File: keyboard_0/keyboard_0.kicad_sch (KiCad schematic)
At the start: 21 parts, among them J1 USB_C_Receptacle_USB2.0, U1 STM32F072CBT6, U2 PRTR5V0U2X, U3 XC6206PxxxMR-Regulator_Linear

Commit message: latest changes - incomplete routing
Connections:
- net A10 renamed ROW0
- net A3 renamed ROW2
- net A4 renamed COL13
- net A5 renamed COL12
- net A6 renamed COL11
- net A7 renamed COL10
- net A8 renamed COL1
- net A9 renamed COL0
- net B0 renamed COL9
- net B1 renamed COL8
- net B10 renamed COL6
- net B11 renamed COL5
- net B12 renamed COL4
- net B13 renamed ROW1
- net B14 renamed COL3
- net B15 renamed COL2
- net B2 renamed COL7

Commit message: connect rest of switches and bring in aux components
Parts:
- added SW1: RotaryEncoder_Switch, PCM_marbastlib-various:ROT_Alps_EC11E-Switch, symbol Device:RotaryEncoder_Switch
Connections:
- net B5 is gone; now on net COL14: U1.41 (PB5)
- net B6 is gone; now on net ROW4: U1.42 (PB6)
- net B7 is gone; now on net ROW3: U1.43 (PB7)
- net COL12: now also U1.13 (PA3); no longer U1.15 (PA5)
- net COL13: now also U1.15 (PA5); no longer U1.14 (PA4)
- net COL4: now also U1.26 (PB13); no longer U1.25 (PB12)
- net GND: now also SW1.C, SW1.S2
- net ROW1: now also U1.25 (PB12); no longer U1.26 (PB13)
- net ROW2: now also U1.14 (PA4); no longer U1.13 (PA3)
- net VBUS: now also SW1.A
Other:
- added sheet LEDs (switches.kicad_sch)

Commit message: bring back switches and separate sub sheets
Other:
- sheet LEDs: file switches.kicad_sch -> led_matrix.kicad_sch
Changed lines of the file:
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@@
 	)
 	(sheet
-		(at 165.1 77.47)
-		(size 50.165 36.83)
+		(at 161.925 73.025)
+		(size 64.135 42.545)
 		(exclude_from_sim no)
 		(in_bom yes)
@@
 		)
 		(property "Sheetname" "LEDs"
-			(at 165.1 76.7584 0)
+			(at 161.925 72.3134 0)
 			(effects
 				(font
@@
 			)
 		)
-		(property "Sheetfile" "switches.kicad_sch"
-			(at 165.1 114.8846 0)
+		(property "Sheetfile" "led_matrix.kicad_sch"
+			(at 161.925 116.1546 0)
 			(effects
 				(font

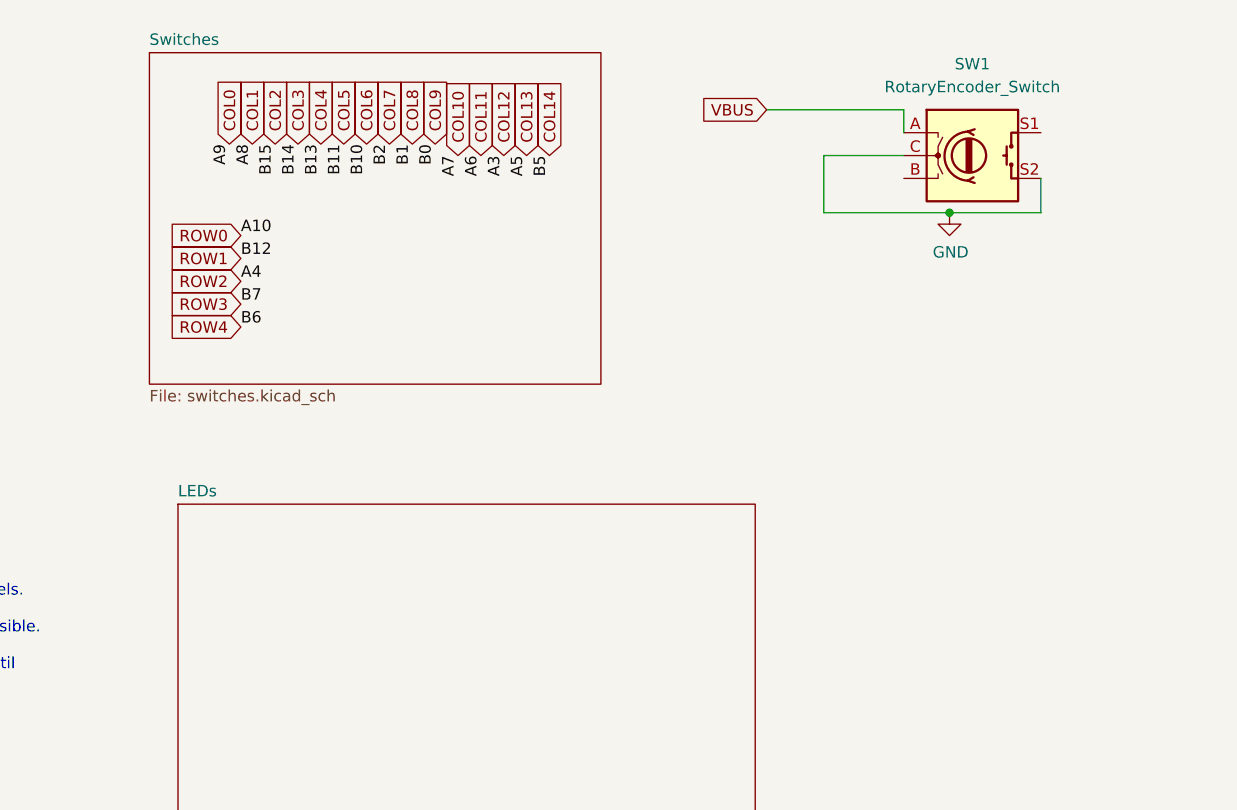
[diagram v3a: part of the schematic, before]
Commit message: add led matrix schematic and finish adding rotary knob
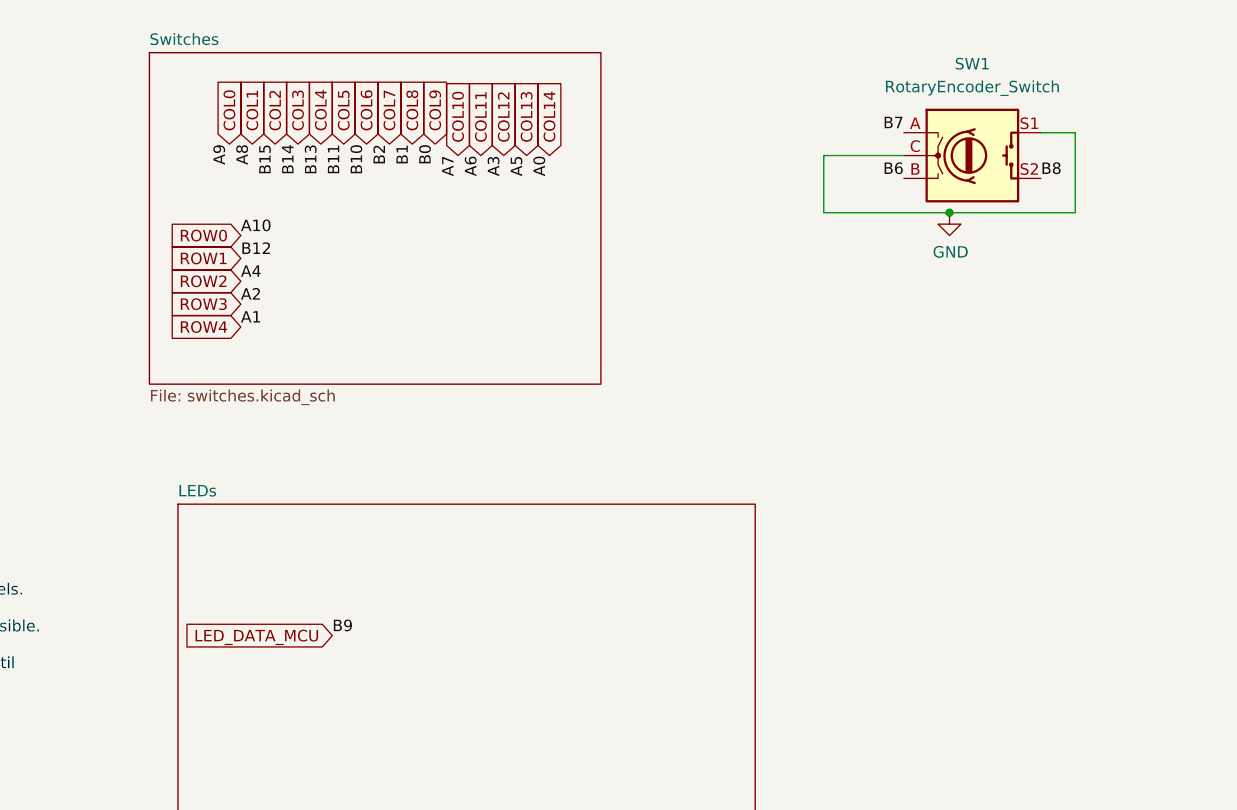
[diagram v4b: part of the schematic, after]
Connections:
- net A0 is gone; now on net COL14: U1.10 (PA0)
- net A1 is gone; now on net ROW4: U1.11 (PA1)
- net A2 is gone; now on net ROW3: U1.12 (PA2)
- net B8: now also SW1.S2
- net COL14: no longer U1.41 (PB5)
- net GND: now also SW1.S1; no longer SW1.S2
- net ROW3: no longer U1.43 (PB7)
- net ROW4: no longer U1.42 (PB6)
- net VBUS: no longer SW1.A
- net B6: now reaches SW1.B
- net B6: now also U1.42 (PB6)
- net B9 renamed LED_DATA_MCU
- new net B5: U1.41 (PB5)
- new net B7: SW1.A, U1.43 (PB7)
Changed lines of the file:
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@@
+	(wire
+		(pts
+			(xy 261.62 31.75) (xy 261.62 40.64)
+		)
+		(stroke
+			(width 0)
+			(type default)
+		)
+	)
 	(wire
 		(pts
@@
 	(wire
 		(pts
-			(xy 257.81 36.83) (xy 257.81 40.64)
-		)
-		(stroke
-			(width 0)
-			(type default)
-		)
-	)
-	(wire
-		(pts
 			(xy 84.455 24.13) (xy 86.995 24.13)
 		)
@@
 	(wire
 		(pts
-			(xy 257.81 40.64) (xy 247.65 40.64)
+			(xy 247.65 40.64) (xy 261.62 40.64)
 		)
 		(stroke
@@
 	(wire
 		(pts
-			(xy 227.33 29.21) (xy 242.57 29.21)
-		)
-		(stroke
-			(width 0)
-			(type default)
-		)
-	)
-	(wire
-		(pts
 			(xy 100.33 60.96) (xy 97.155 60.96)
 		)
@@
 	(wire
 		(pts
-			(xy 242.57 29.21) (xy 242.57 31.75)
-		)
-		(stroke
-			(width 0)
-			(type default)
-		)
-	)
-	(wire
-		(pts
 			(xy 49.53 156.845) (xy 49.53 155.575)
 		)
@@
 		(pts
 			(xy 48.26 151.765) (xy 49.53 151.765)
+		)
+		(stroke
+			(width 0)
+			(type default)
+		)
+	)
+	(wire
+		(pts
+			(xy 257.81 31.75) (xy 261.62 31.75)
 		)
 		(stroke
@@
 		)
 	)
-	(label "B6"
-		(at 168.91 53.34 0)
-		(effects
-			(font
-				(size 1.27 1.27)
-			)
-			(justify left bottom)
-		)
-	)
 	(label "A5"
 		(at 200.66 34.29 270)
@@
 		)
 	)
+	(label "A2"
+		(at 168.91 50.8 0)
+		(effects
+			(font
+				(size 1.27 1.27)
+			)
+			(justify left bottom)
+		)
+	)
 	(label "B7"
 		(at 60.96 76.2 180)
@@
 		)
 	)
-	(label "B7"
-		(at 168.91 50.8 0)
-		(effects
-			(font
-				(size 1.27 1.27)
-			)
-			(justify left bottom)
-		)
-	)
 	(label "B5"
 		(at 60.96 71.12 180)
@@
 		)
 	)
+	(label "A0"
+		(at 203.2 34.29 270)
+		(effects
+			(font
+				(size 1.27 1.27)
+			)
+			(justify right bottom)
+		)
+	)
+	(label "B9"
+		(at 179.07 87.63 0)
+		(effects
+			(font
+				(size 1.27 1.27)
+			)
+			(justify left bottom)
+		)
+	)
 	(label "B10"
 		(at 60.96 83.82 180)
@@
 		)
 	)
+	(label "B8"
+		(at 257.81 36.83 0)
+		(effects
+			(font
+				(size 1.27 1.27)
+			)
+			(justify left bottom)
+		)
+	)
+	(label "B7"
+		(at 242.57 31.75 180)
+		(effects
+			(font
+				(size 1.27 1.27)
+			)
+			(justify right bottom)
+		)
+	)
 	(label "B14"
 		(at 175.26 33.02 270)
@@
 		)
 	)
-	(label "B5"
-		(at 203.2 34.29 270)
-		(effects
-			(font
-				(size 1.27 1.27)
-			)
-			(justify right bottom)
-		)
-	)
 	(label "A0"
 		(at 98.425 30.48 0)
@@
 			)
 			(justify left bottom)
+		)
+	)
+	(label "A1"
+		(at 168.91 53.34 0)
+		(effects
+			(font
+				(size 1.27 1.27)
+			)
+			(justify left bottom)
+		)
+	)
+	(label "B6"
+		(at 242.57 36.83 180)
+		(effects
+			(font
+				(size 1.27 1.27)
+			)
+			(justify right bottom)
 		)
 	)
@@
 		)
 	)
-	(global_label "VBUS"
-		(shape input)
-		(at 227.33 29.21 180)
-		(fields_autoplaced yes)
-		(effects
-			(font
-				(size 1.27 1.27)
-			)
-			(justify right)
-		)
-		(property "Intersheetrefs" "${INTERSHEET_REFS}"
-			(at 219.5256 29.21 0)
-			(effects
-				(font
-					(size 1.27 1.27)
-				)
-				(justify right)
-				(hide yes)
-			)
-		)
-	)
 	(global_label "COL7"
 		(shape input)
@@
 			(effects
 				(font
+					(size 1.27 1.27)
+				)
+				(justify right)
+				(hide yes)
+			)
+		)
+	)
+	(global_label "LED_DATA_MCU"
+		(shape input)
+		(at 179.07 87.63 180)
+		(fields_autoplaced yes)
+		(effects
+			(font
+				(size 1.27 1.27)
+			)
+			(justify right)
+		)
+		(property "Intersheetrefs" "${INTERSHEET_REFS}"
+			(at 162.2358 87.63 0)
+			(effects
+				(font
